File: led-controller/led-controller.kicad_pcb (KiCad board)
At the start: 2 copper layers, 38.1 x 41.9 mm, 19 parts, among them IC1 ATMEGA1284P-M, P1 CONN_01X05, P2 Conn, P3 CONN_02X03, U1 TLV70012DDC, Y1 16MHz

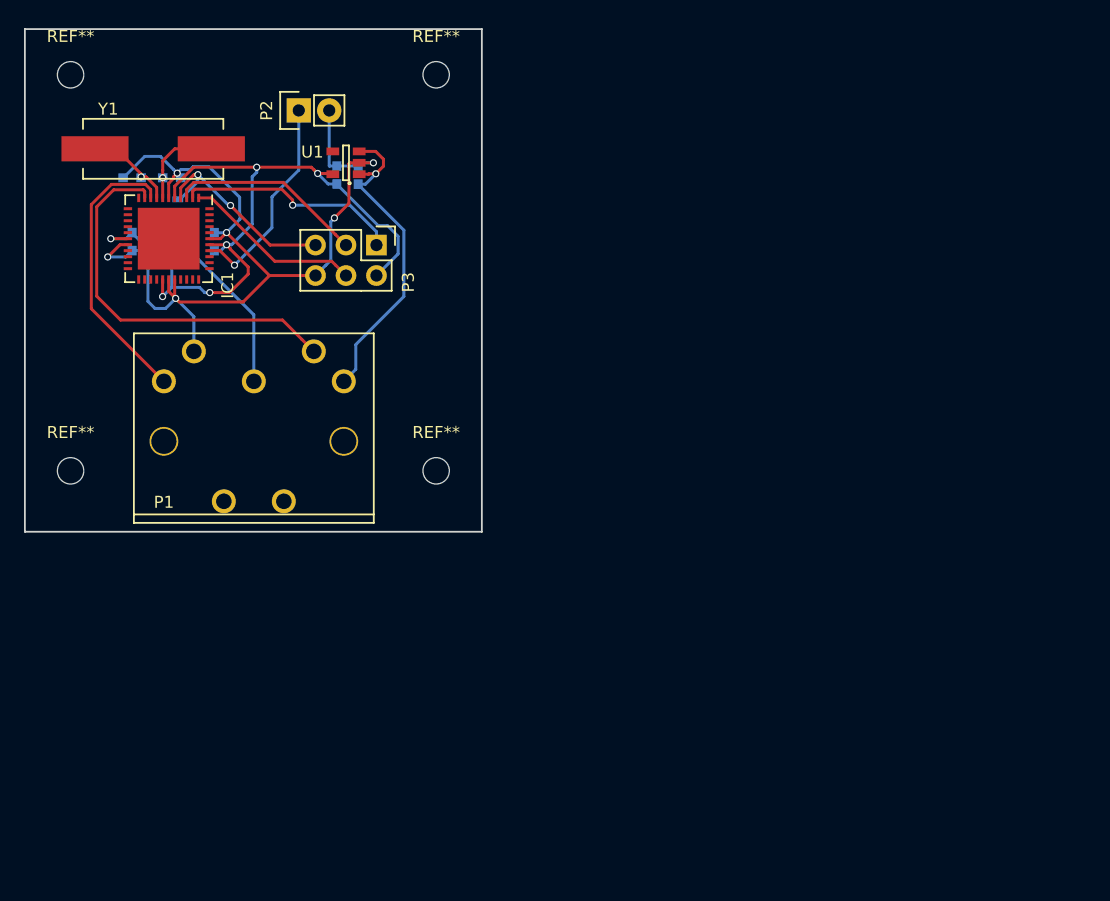
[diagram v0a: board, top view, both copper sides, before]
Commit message: Addition of LED controller and screw terminal element
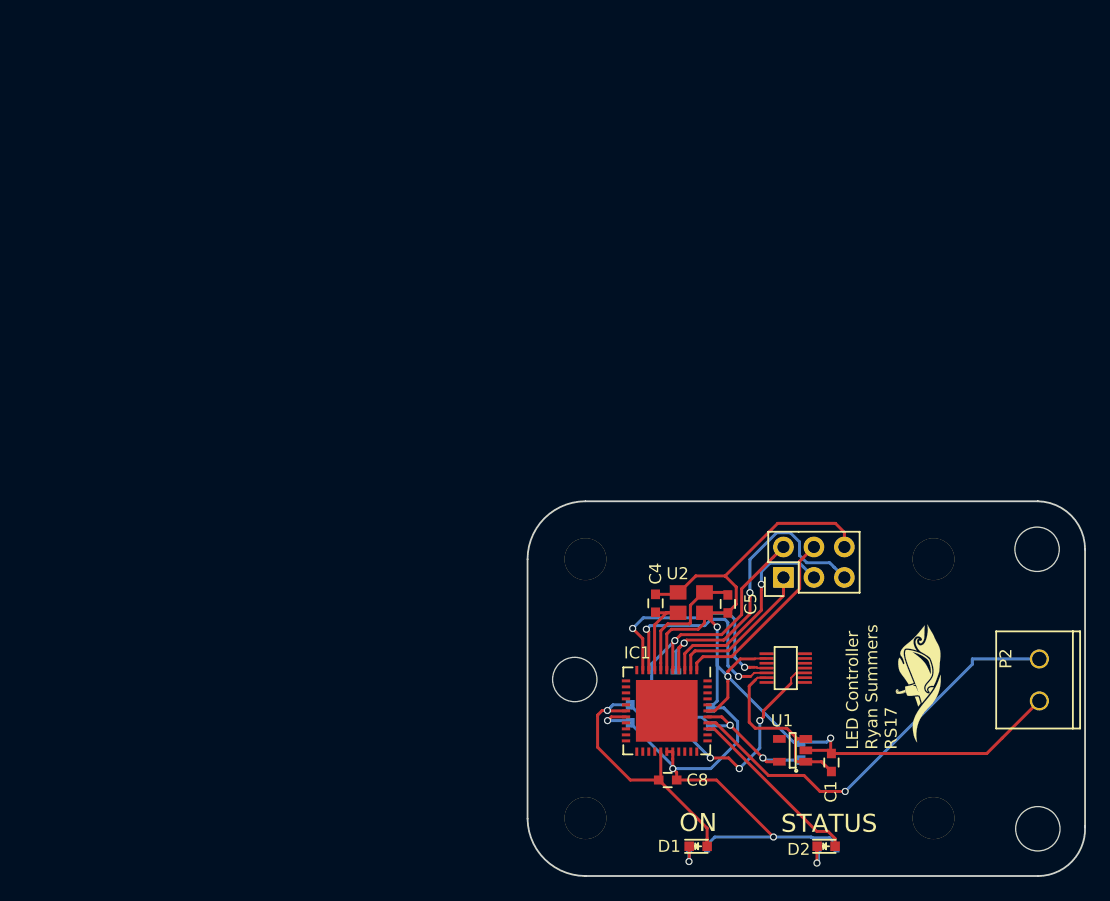
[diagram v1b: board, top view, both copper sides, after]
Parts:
- removed the REF** at (119.4, 124.5)
- removed the REF** at (88.9, 124.5)
- removed the REF** at (88.9, 91.4)
- removed the REF** at (119.4, 91.4)
- removed Y1: 16MHz, Crystals:Crystal_HC49-SD_SMD
- added C8: 4.7u, Capacitors_SMD:C_0603, F.Cu at (138.7, 150.2)
- added D1: LED, LEDs:LED_0603, F.Cu at (141.2, 155.8)
- added D2: LED, LEDs:LED_0603, F.Cu at (151.9, 155.8)
- added G***: LOGO, robosub_footprints:robosub_logo-medium, F.Cu at (159.7, 142.1)
- added P4: Spacer, robosub_footprints:1.5mm-spacer, F.Cu at (131.8, 153.4)
- added P5: Spacer, robosub_footprints:1.5mm-spacer, F.Cu at (131.8, 131.8)
- added P6: Spacer, robosub_footprints:1.5mm-spacer, F.Cu at (160.8, 131.8)
- added P7: CONN_02X03, Pin_Headers:Pin_Header_Straight_2x03, F.Cu at (148.3, 133.3)
- added R3: 65, Resistors_SMD:R_0603, B.Cu at (141.2, 155.8)
- added R4: 65, Resistors_SMD:R_0603, B.Cu at (152.0, 155.8)
- added REF**: MountingHole_3.7mm, Mounting_Holes:MountingHole_3.7mm, F.Cu at (130.9, 141.9)
- added REF**: MountingHole_3.7mm, Mounting_Holes:MountingHole_3.7mm, F.Cu at (169.5, 131.0)
- added REF**: MountingHole_3.7mm, Mounting_Holes:MountingHole_3.7mm, F.Cu at (169.5, 154.3)
- added U2: TSX-3225, robosub_footprints:DFN-4, F.Cu at (140.7, 135.4)
- C1: moved to F.Cu
- C4, C5: value 30pF -> 18p; moved to F.Cu
- C6, C7: value C -> 100n
- P1: value CONN_01X05 -> Mezzanine-Header; footprint robosub_footprints:cui-5-board-f -> robosub_footprints:DF40C-10DP-Header
- P2: footprint Pin_Headers:Pin_Header_Straight_1x02 -> robosub_footprints:Screw-Terminal-2-3.5mm
- P3: value CONN_02X03 -> Spacer; footprint Pin_Headers:Pin_Header_Straight_2x03 -> robosub_footprints:1.5mm-spacer
- moved P2 77.9 mm to (169.7, 141.9), turned to 270 degrees
- moved P3 66.6 mm to (160.8, 153.4)
- moved C1 62.9 mm to (152.3, 148.8)
- moved C2 61.7 mm to (149.8, 147.8)
- moved U1 61.5 mm to (149.1, 147.8)
- moved C5 61.1 mm to (143.7, 135.6), turned to 270 degrees
- moved C6 57.3 mm to (142.2, 145.0)
- moved C3 57.2 mm to (140.6, 145.0)
- moved IC1 57.2 mm to (138.6, 144.5)
- moved R2 57.2 mm to (139.4, 141.9)
- moved C7 57.2 mm to (135.6, 144.7)
- moved R1 57.2 mm to (138.9, 145.0)
- moved P1 55.2 mm to (148.5, 140.9), turned to 90 degrees
- moved C4 53.7 mm to (137.7, 135.5), turned to 90 degrees
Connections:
- net /Sheet580A8768/PA0 renamed /signal
- net /Sheet580A8768/Tx_CPU renamed /TX_CPU
- C3 pad 2: /Sheet580A8768/DTR -> /DTR
- C4 pad 1: GND -> Net-(C4-Pad1)
- C4 pad 2: Net-(C4-Pad2) -> GND
- IC1 pad 10: /Sheet580A8768/Rx_CPU -> /RX_CPU
- IC1 pad 36: (no net) -> /Sheet580A8768/DBG_LED
- IC1 pad 7: Net-(C4-Pad2) -> Net-(C5-Pad1)
- IC1 pad 8: Net-(C5-Pad1) -> Net-(C4-Pad1)
- P1 pad 2: /Sheet580A8768/DTR -> (no net)
- P1 pad 4: /Sheet580A8768/Rx_CPU -> /DTR
- P1 pad 5: GND -> /RX_CPU
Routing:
- net GND: track 80.9 -> 129.5 mm
- net /Sheet580A8768/Rx_CPU: track 32.7 -> 0.00 mm
- net /RX_CPU: track 0.00 -> 19.3 mm, vias 0 -> 2
- net /signal: track 17.7 -> 34.9 mm
- net /DTR: track 0.00 -> 16.8 mm, vias 0 -> 3
- net /Sheet580A8768/DBG_LED: track 0.00 -> 15.1 mm
- net /Sheet580A8768/DTR: track 12.7 -> 0.00 mm
- net +5V: track 27.1 -> 16.0 mm, vias 1 -> 0
- net /Sheet580A8768/~RST: track 17.8 -> 27.8 mm
- net Net-(C4-Pad1): track 0.00 -> 8.05 mm
- net Net-(C4-Pad2): track 7.58 -> 0.00 mm, vias 1 -> 0
- net +3V3: track 61.6 -> 69.0 mm, vias 6 -> 4
- net /Sheet580A8768/MISO: track 18.8 -> 12.5 mm, vias 1 -> 0
- net /TX_CPU: track 23.8 -> 18.1 mm, vias 0 -> 2
- net Net-(C5-Pad1): track 7.58 -> 11.2 mm, vias 1 -> 0
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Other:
- board size 38.1 x 41.9 mm -> 46.5 x 31.2 mm
- net class Default: clearance 0.2 -> 0.16
- rule pad_to_mask_clearance: 0.2 -> 0
- rule trace_clearance: 0.2 -> 0.16
- board text added: "LED Controller Ryan Summers RS17"
- board text added: "ON"
- board text added: "STATUS"

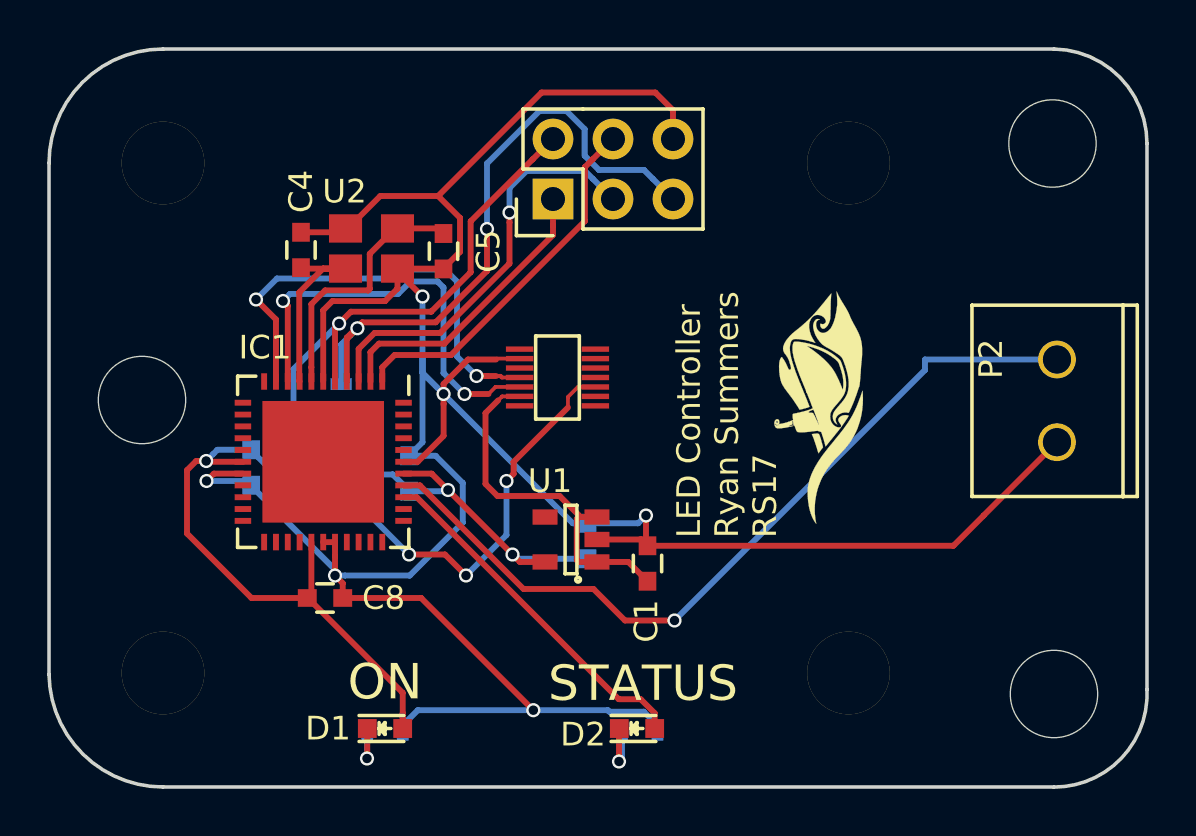
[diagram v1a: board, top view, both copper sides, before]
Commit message: Update post review of LED controller board
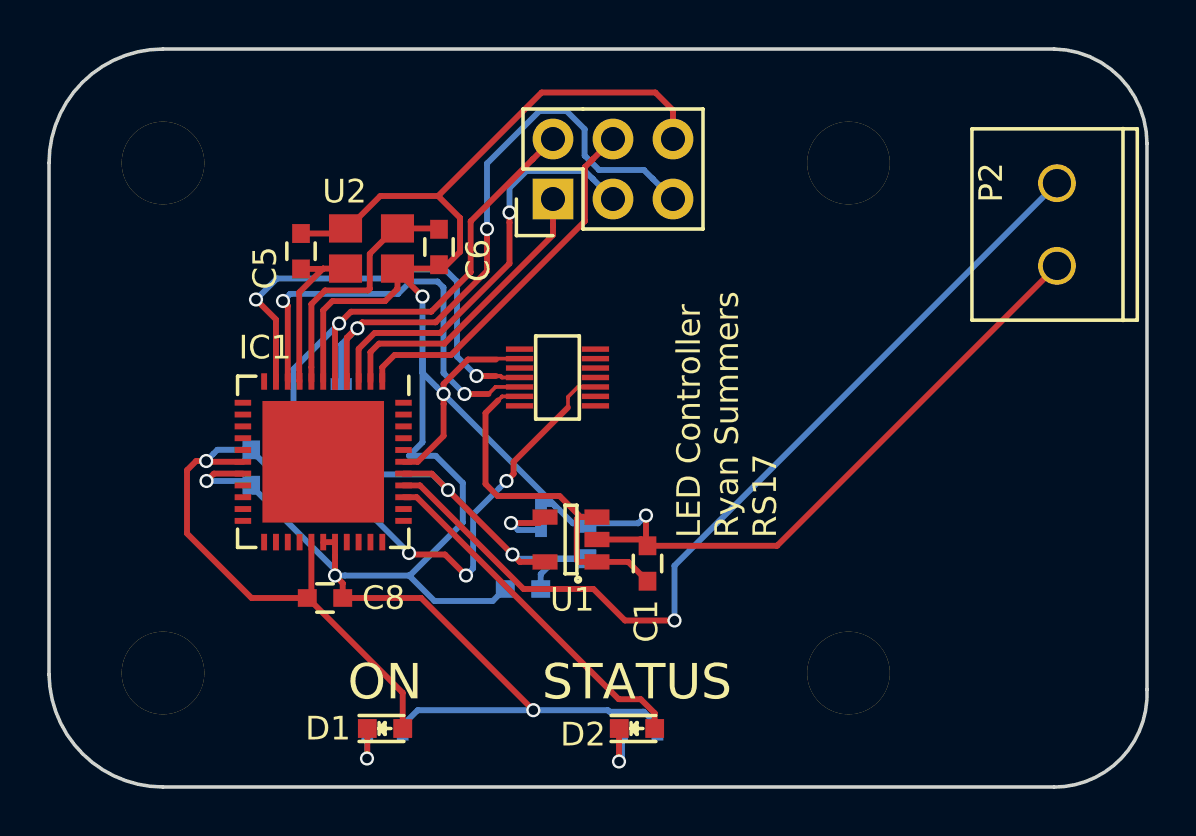
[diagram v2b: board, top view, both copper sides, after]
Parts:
- removed G***: LOGO, robosub_footprints:robosub_logo-medium
- removed REF** (x3): MountingHole_3.7mm, Mounting_Holes:MountingHole_3.7mm
- added C9: 4.7u, Capacitors_SMD:C_0603, B.Cu at (147.1, 149.9)
- C3: value 100nF -> 100p; footprint Capacitors_SMD:C_0603 -> Capacitors_SMD:C_0402
- C4: value 18p -> 100nF; moved to B.Cu
- C6: value 100n -> 18p; moved to F.Cu
- C8: value 4.7u -> 100n
- U1: value TLV70012DDC -> AP2210; footprint SOT-23-5 -> TO_SOT_Packages_SMD:SOT-23-5
- moved C4 10.0 mm to (140.7, 145.0), turned to 270 degrees
- moved C6 9.67 mm to (143.5, 135.4), turned to 270 degrees
- moved P2 7.47 mm to (169.7, 134.4)
- moved C3 7.42 mm to (147.8, 146.8), turned to 90 degrees
- moved C5 6.03 mm to (137.7, 135.6), turned to 90 degrees
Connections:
- C3 pad 2: /DTR -> GND
- C4 pad 2: GND -> /DTR
- C6 pad 1: +3V3 -> Net-(C6-Pad1)
- IC1 pad 7: Net-(C5-Pad1) -> Net-(C6-Pad1)
- IC1 pad 8: Net-(C4-Pad1) -> Net-(C5-Pad1)
- R1 pad 2: Net-(C3-Pad1) -> Net-(C4-Pad1)
- R2 pad 2: Net-(C3-Pad1) -> Net-(C4-Pad1)
- U1 pad 4: (no net) -> Net-(C3-Pad1)
- U2 pad 1: Net-(C5-Pad1) -> Net-(C6-Pad1)
- U2 pad 3: Net-(C4-Pad1) -> Net-(C5-Pad1)
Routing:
- net Net-(C6-Pad1): track 0.00 -> 10.9 mm
- net GND: track 129.5 -> 138.1 mm
- net Net-(C4-Pad1): track 8.05 -> 3.54 mm
- net /signal: track 34.9 -> 39.1 mm
- net Net-(C5-Pad1): track 11.2 -> 7.09 mm
- net +3V3: track 69.0 -> 71.3 mm
- net Net-(C3-Pad1): track 3.54 -> 2.94 mm, vias 0 -> 1

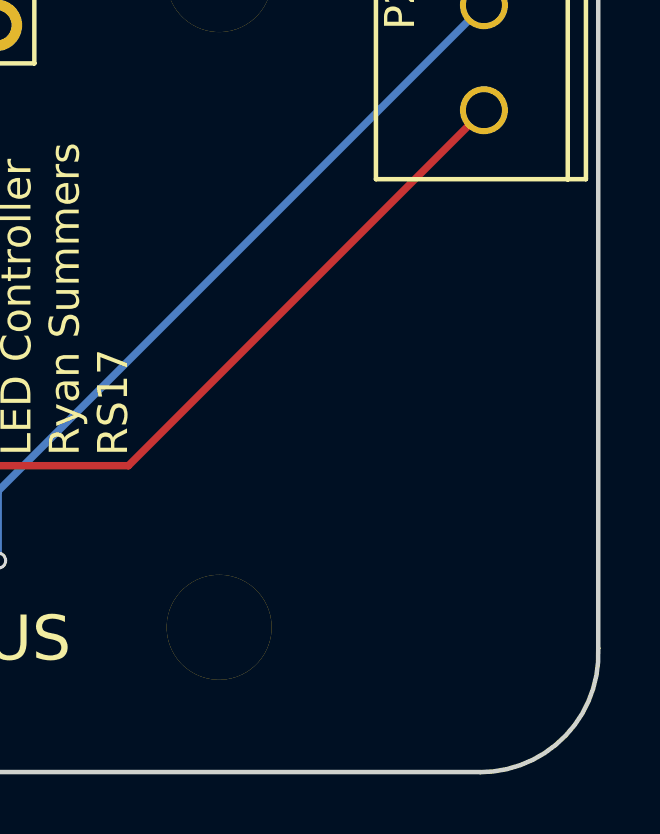
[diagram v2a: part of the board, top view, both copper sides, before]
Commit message: Added logo to LED Controller
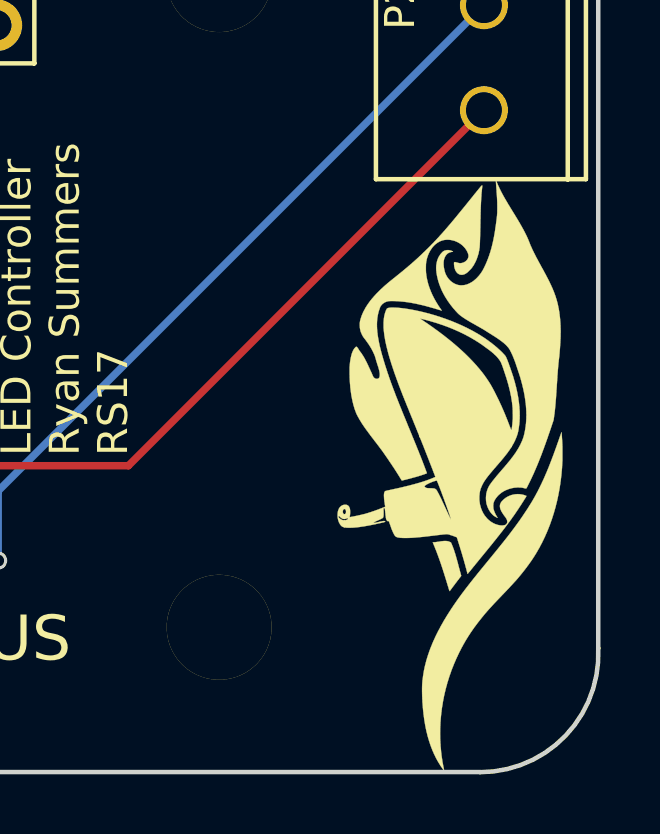
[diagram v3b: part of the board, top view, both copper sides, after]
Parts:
- added G***: LOGO, robosub_footprints:robosub_logo-large, F.Cu at (168.8, 148.2)
